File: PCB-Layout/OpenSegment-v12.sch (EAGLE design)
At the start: 48 parts, among them Q1 PNP, Q10 MMBT2222, Q11 MMBT2222, Q12 MMBT2222, Q2 PNP, Q3 PNP, Q4 PNP, Q5 PNP, Q6 PNP, Q7 PNP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

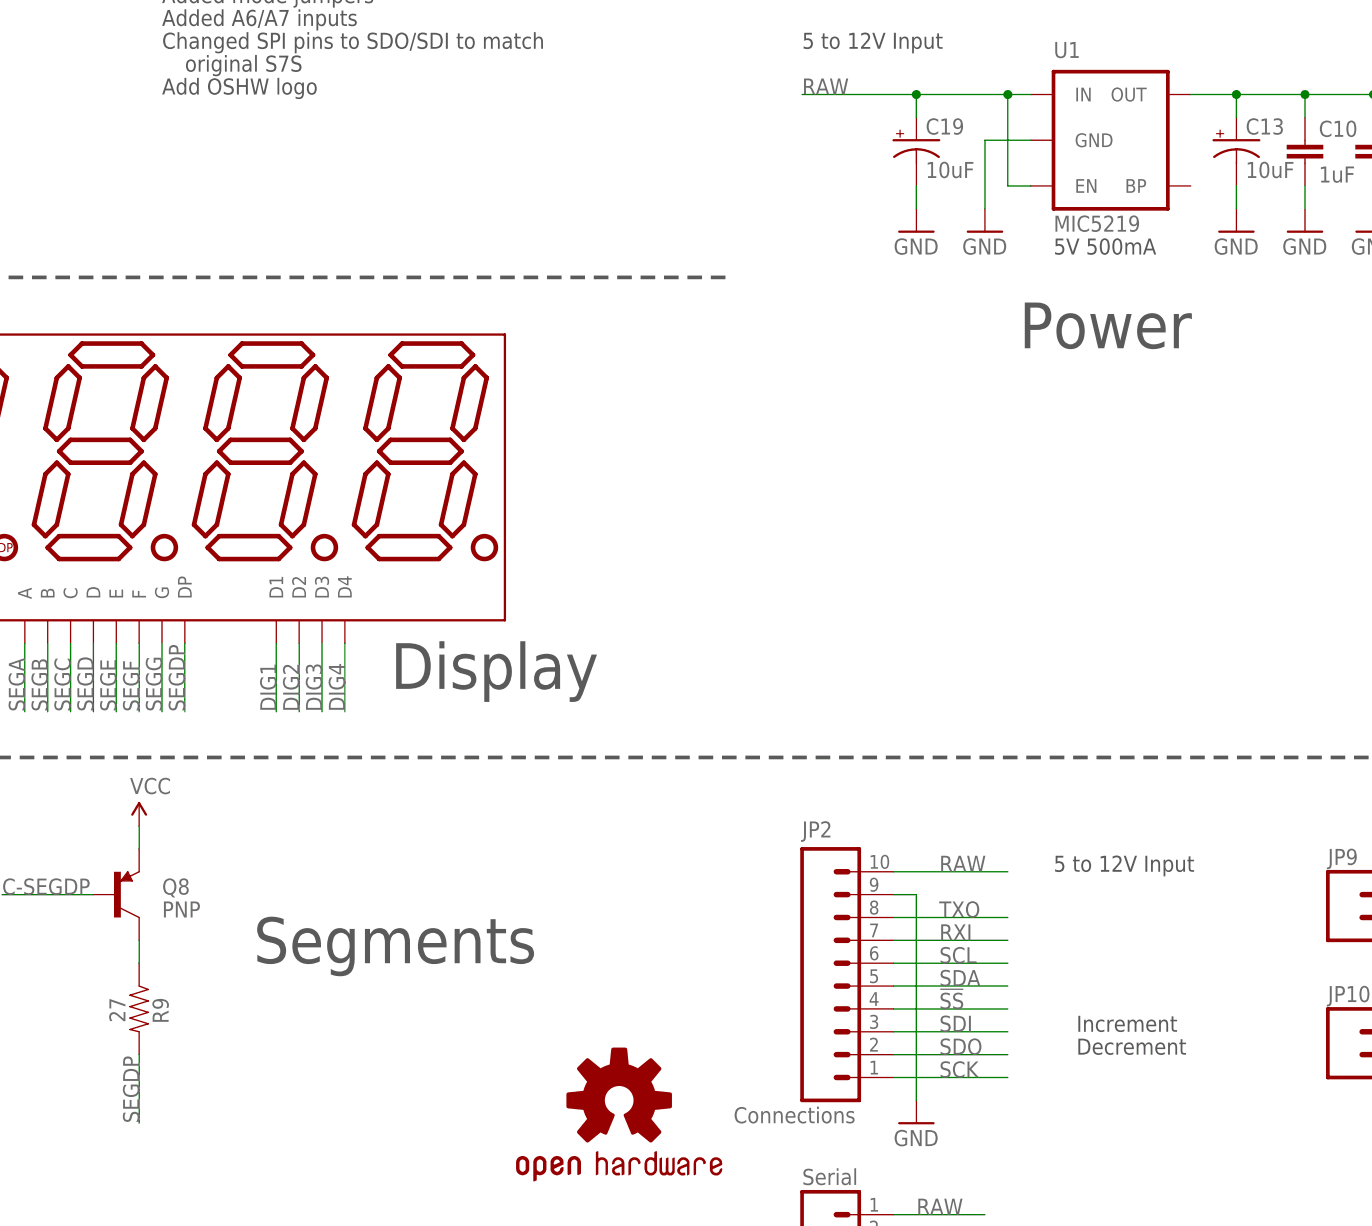
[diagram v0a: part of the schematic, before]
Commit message: Added I2C gang pins, silk color squares, adjusted 10uF cap spot.
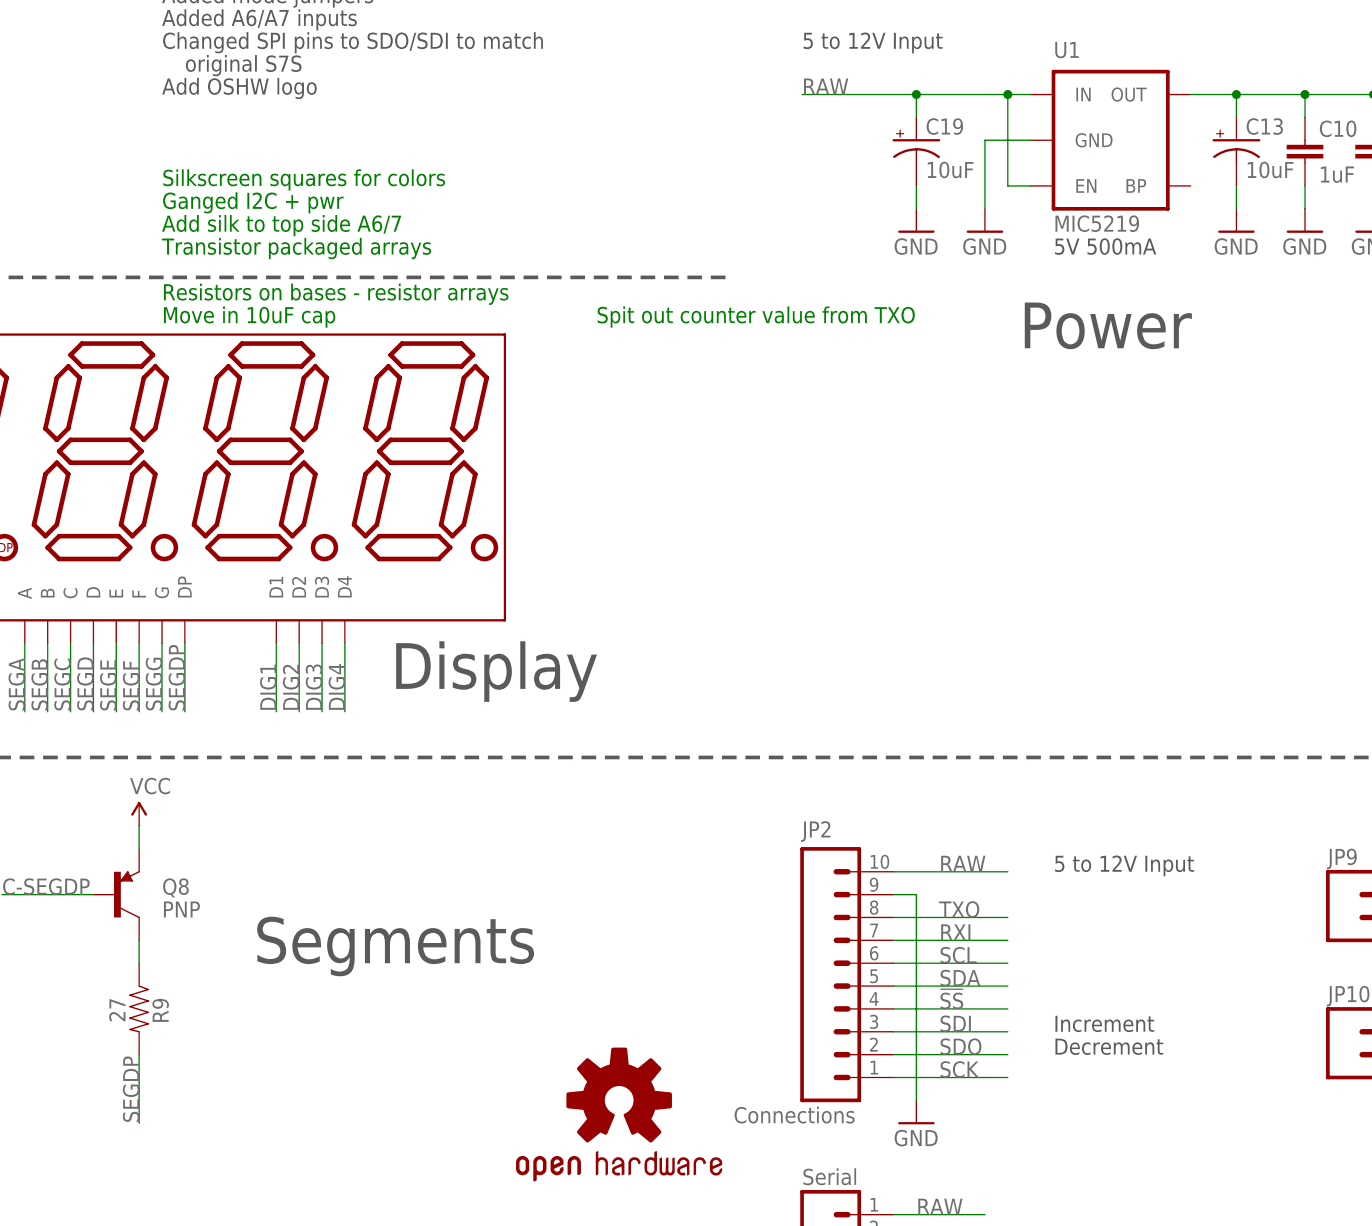
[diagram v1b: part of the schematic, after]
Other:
- note added: "Add silk to top side A6/7"
- note added: "Ganged I2C + pwr"
- note added: "Move in 10uF cap"
- note added: "Resistors on bases - resistor arrays"
- note added: "Silkscreen squares for colors"
- note added: "Spit out counter value from TXO"
- note added: "Transistor packaged arrays"
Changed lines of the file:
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@@
 <grid distance="0.1" unitdist="inch" unit="inch" style="lines" multiple="1" display="no" altdistance="0.01" altunitdist="inch" altunit="inch"/>
 <layers>
-<layer number="1" name="Top" color="4" fill="1" visible="yes" active="no"/>
-<layer number="2" name="Route2" color="1" fill="3" visible="yes" active="no"/>
-<layer number="3" name="Route3" color="4" fill="3" visible="yes" active="no"/>
-<layer number="4" name="Route4" color="1" fill="4" visible="yes" active="no"/>
-<layer number="5" name="Route5" color="4" fill="4" visible="yes" active="no"/>
-<layer number="6" name="Route6" color="1" fill="8" visible="yes" active="no"/>
-<layer number="7" name="Route7" color="4" fill="8" visible="yes" active="no"/>
-<layer number="8" name="Route8" color="1" fill="2" visible="yes" active="no"/>
-<layer number="9" name="Route9" color="4" fill="2" visible="yes" active="no"/>
-<layer number="10" name="Route10" color="1" fill="7" visible="yes" active="no"/>
-<layer number="11" name="Route11" color="4" fill="7" visible="yes" active="no"/>
-<layer number="12" name="Route12" color="1" fill="5" visible="yes" active="no"/>
-<layer number="13" name="Route13" color="4" fill="5" visible="yes" active="no"/>
-<layer number="14" name="Route14" color="1" fill="6" visible="yes" active="no"/>
-<layer number="15" name="Route15" color="4" fill="6" visible="yes" active="no"/>
-<layer number="16" name="Bottom" color="1" fill="1" visible="yes" active="no"/>
-<layer number="17" name="Pads" color="2" fill="1" visible="yes" active="no"/>
-<layer number="18" name="Vias" color="2" fill="1" visible="yes" active="no"/>
-<layer number="19" name="Unrouted" color="6" fill="1" visible="yes" active="no"/>
-<layer number="20" name="Dimension" color="24" fill="1" visible="yes" active="no"/>
-<layer number="21" name="tPlace" color="16" fill="1" visible="yes" active="no"/>
-<layer number="22" name="bPlace" color="14" fill="1" visible="yes" active="no"/>
-<layer number="23" name="tOrigins" color="15" fill="1" visible="yes" active="no"/>
-<layer number="24" name="bOrigins" color="15" fill="1" visible="yes" active="no"/>
-<layer number="25" name="tNames" color="7" fill="1" visible="yes" active="no"/>
-<layer number="26" name="bNames" color="7" fill="1" visible="yes" active="no"/>
-<layer number="27" name="tValues" color="7" fill="1" visible="yes" active="no"/>
-<layer number="28" name="bValues" color="7" fill="1" visible="yes" active="no"/>
+<layer number="1" name="Top" color="4" fill="1" visible="no" active="no"/>
+<layer number="2" name="Route2" color="1" fill="3" visible="no" active="no"/>
+<layer number="3" name="Route3" color="4" fill="3" visible="no" active="no"/>
+<layer number="4" name="Route4" color="1" fill="4" visible="no" active="no"/>
+<layer number="5" name="Route5" color="4" fill="4" visible="no" active="no"/>
+<layer number="6" name="Route6" color="1" fill="8" visible="no" active="no"/>
+<layer number="7" name="Route7" color="4" fill="8" visible="no" active="no"/>
+<layer number="8" name="Route8" color="1" fill="2" visible="no" active="no"/>
+<layer number="9" name="Route9" color="4" fill="2" visible="no" active="no"/>
+<layer number="10" name="Route10" color="1" fill="7" visible="no" active="no"/>
+<layer number="11" name="Route11" color="4" fill="7" visible="no" active="no"/>
+<layer number="12" name="Route12" color="1" fill="5" visible="no" active="no"/>
+<layer number="13" name="Route13" color="4" fill="5" visible="no" active="no"/>
+<layer number="14" name="Route14" color="1" fill="6" visible="no" active="no"/>
+<layer number="15" name="Route15" color="4" fill="6" visible="no" active="no"/>
+<layer number="16" name="Bottom" color="1" fill="1" visible="no" active="no"/>
+<layer number="17" name="Pads" color="2" fill="1" visible="no" active="no"/>
+<layer number="18" name="Vias" color="2" fill="1" visible="no" active="no"/>
+<layer number="19" name="Unrouted" color="6" fill="1" visible="no" active="no"/>
+<layer number="20" name="Dimension" color="24" fill="1" visible="no" active="no"/>
+<layer number="21" name="tPlace" color="16" fill="1" visible="no" active="no"/>
+<layer number="22" name="bPlace" color="14" fill="1" visible="no" active="no"/>
+<layer number="23" name="tOrigins" color="15" fill="1" visible="no" active="no"/>
+<layer number="24" name="bOrigins" color="15" fill="1" visible="no" active="no"/>
+<layer number="25" name="tNames" color="7" fill="1" visible="no" active="no"/>
+<layer number="26" name="bNames" color="7" fill="1" visible="no" active="no"/>
+<layer number="27" name="tValues" color="7" fill="1" visible="no" active="no"/>
+<layer number="28" name="bValues" color="7" fill="1" visible="no" active="no"/>
 <layer number="29" name="tStop" color="7" fill="3" visible="no" active="no"/>
 <layer number="30" name="bStop" color="7" fill="6" visible="no" active="no"/>
@@
 <layer number="35" name="tGlue" color="7" fill="4" visible="no" active="no"/>
 <layer number="36" name="bGlue" color="7" fill="5" visible="no" active="no"/>
-<layer number="37" name="tTest" color="7" fill="1" visible="yes" active="no"/>
-<layer number="38" name="bTest" color="7" fill="1" visible="yes" active="no"/>
+<layer number="37" name="tTest" color="7" fill="1" visible="no" active="no"/>
+<layer number="38" name="bTest" color="7" fill="1" visible="no" active="no"/>
 <layer number="39" name="tKeepout" color="4" fill="11" visible="no" active="no"/>
 <layer number="40" name="bKeepout" color="1" fill="11" visible="no" active="no"/>
@@
 <layer number="44" name="Drills" color="7" fill="1" visible="no" active="no"/>
 <layer number="45" name="Holes" color="7" fill="1" visible="no" active="no"/>
-<layer number="46" name="Milling" color="3" fill="1" visible="yes" active="no"/>
-<layer number="47" name="Measures" color="7" fill="1" visible="yes" active="no"/>
-<layer number="48" name="Document" color="7" fill="1" visible="yes" active="no"/>
-<layer number="49" name="Reference" color="7" fill="1" visible="yes" active="no"/>
-<layer number="50" name="dxf" color="7" fill="1" visible="yes" active="no"/>
-<layer number="51" name="tDocu" color="6" fill="1" visible="yes" active="no"/>
-<layer number="52" name="bDocu" color="7" fill="1" visible="yes" active="no"/>
-<layer number="53" name="tGND_GNDA" color="7" fill="9" visible="yes" active="no"/>
-<layer number="54" name="bGND_GNDA" color="1" fill="9" visible="yes" active="no"/>
-<layer number="56" name="wert" color="7" fill="1" visible="yes" active="no"/>
+<layer number="46" name="Milling" color="3" fill="1" visible="no" active="no"/>
+<layer number="47" name="Measures" color="7" fill="1" visible="no" active="no"/>
+<layer number="48" name="Document" color="7" fill="1" visible="no" active="no"/>
+<layer number="49" name="Reference" color="7" fill="1" visible="no" active="no"/>
+<layer number="50" name="dxf" color="7" fill="1" visible="no" active="no"/>
+<layer number="51" name="tDocu" color="6" fill="1" visible="no" active="no"/>
+<layer number="52" name="bDocu" color="7" fill="1" visible="no" active="no"/>
+<layer number="53" name="tGND_GNDA" color="7" fill="9" visible="no" active="no"/>
+<layer number="54" name="bGND_GNDA" color="1" fill="9" visible="no" active="no"/>
+<layer number="56" name="wert" color="7" fill="1" visible="no" active="no"/>
 <layer number="91" name="Nets" color="2" fill="1" visible="yes" active="yes"/>
 <layer number="92" name="Busses" color="1" fill="1" visible="yes" active="yes"/>
@@
 <text x="6.096" y="112.014" size="1.778" layer="97" rot="R90">Close Jumper For:</text>
 <text x="25.908" y="116.84" size="1.778" layer="97" rot="R90">Meter Mode</text>
-<text x="287.02" y="53.34" size="1.778" layer="97">Increment</text>
-<text x="287.02" y="50.8" size="1.778" layer="97">Decrement</text>
+<text x="284.48" y="53.34" size="1.778" layer="97">Increment</text>
+<text x="284.48" y="50.8" size="1.778" layer="97">Decrement</text>
 <text x="185.42" y="167.64" size="1.778" layer="97">Added mode jumpers</text>
 <wire x1="-33.02" y1="83.82" x2="-33.02" y2="0" width="0.4064" layer="97" style="shortdash"/>
@@
 <text x="185.42" y="175.26" size="1.778" layer="97">R = 38.3 Ohm</text>
 <text x="185.42" y="172.72" size="1.778" layer="97">Measurements show 10mA. Changing to 27 Ohm</text>
+<text x="185.42" y="147.32" size="1.778" layer="91">Silkscreen squares for colors</text>
+<text x="185.42" y="144.78" size="1.778" layer="91">Ganged I2C + pwr</text>
+<text x="185.42" y="142.24" size="1.778" layer="91">Add silk to top side A6/7</text>
+<text x="185.42" y="139.7" size="1.778" layer="91">Transistor packaged arrays</text>
+<text x="185.42" y="134.62" size="1.778" layer="91">Resistors on bases - resistor arrays</text>
+<text x="185.42" y="132.08" size="1.778" layer="91">Move in 10uF cap</text>
+<text x="233.68" y="132.08" size="1.778" layer="91">Spit out counter value from TXO</text>
 </plain>
 <instances>
